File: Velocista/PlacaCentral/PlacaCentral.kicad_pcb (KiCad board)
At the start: 2 copper layers, 39 parts, among them J1 AUX1, J10 TB6612FNG_A, J11 MOT_IZQ, J12 MOT_DER, J13 DIST_DCHA, J14 TB6612FNG_B, J15 LIPO_1S_A, J16 LIPO_1S_B, J2 AUX2, J3 AUX3, J4 AUX4, J5 HC-05, J6 Sensores_linea, J7 DIST_IZQ, J8 DIST_FRONT, J9 LIPO_2S, SW1 B1, SW2 B2, SW3 SW_DPDT_x2, U1 PCF8574, U2 DC-DC_BuckModule

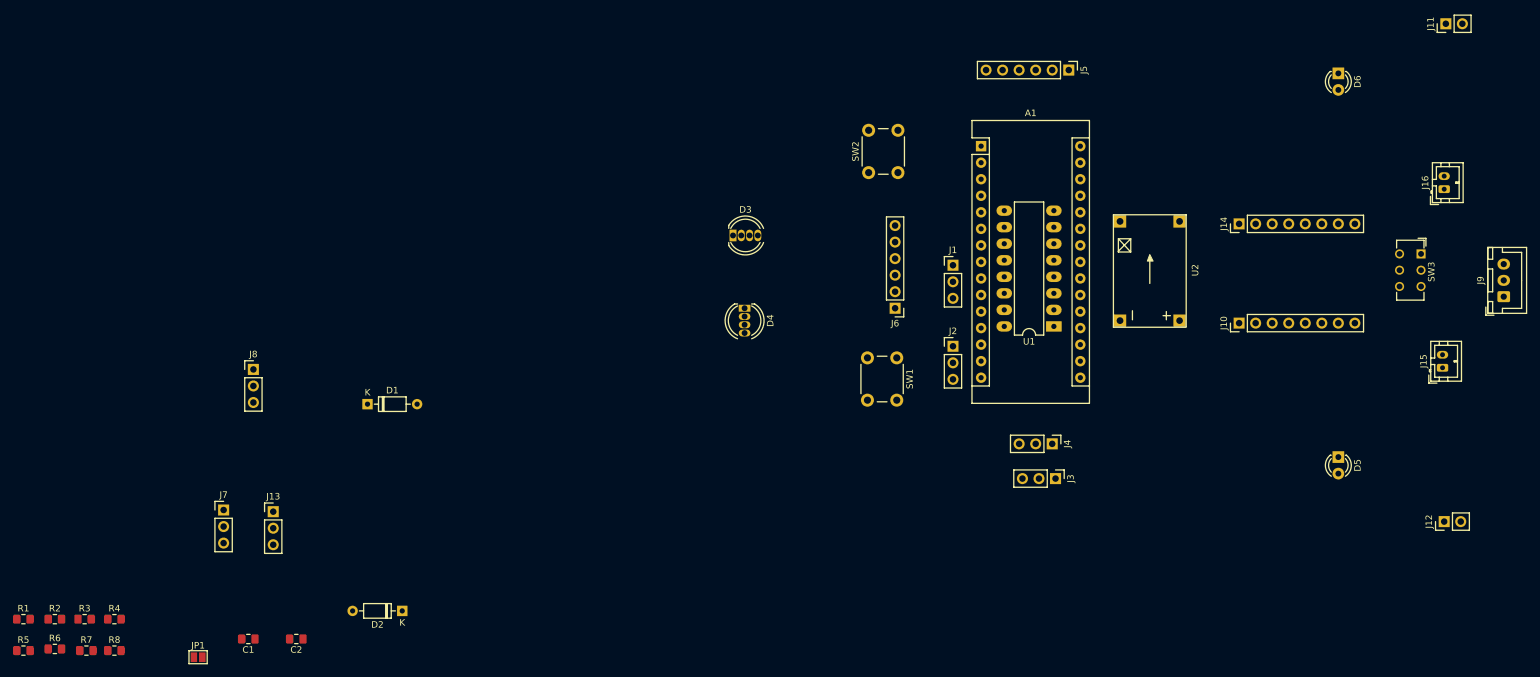
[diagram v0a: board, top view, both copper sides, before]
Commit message: Terminada distribución de componentes y enrutado
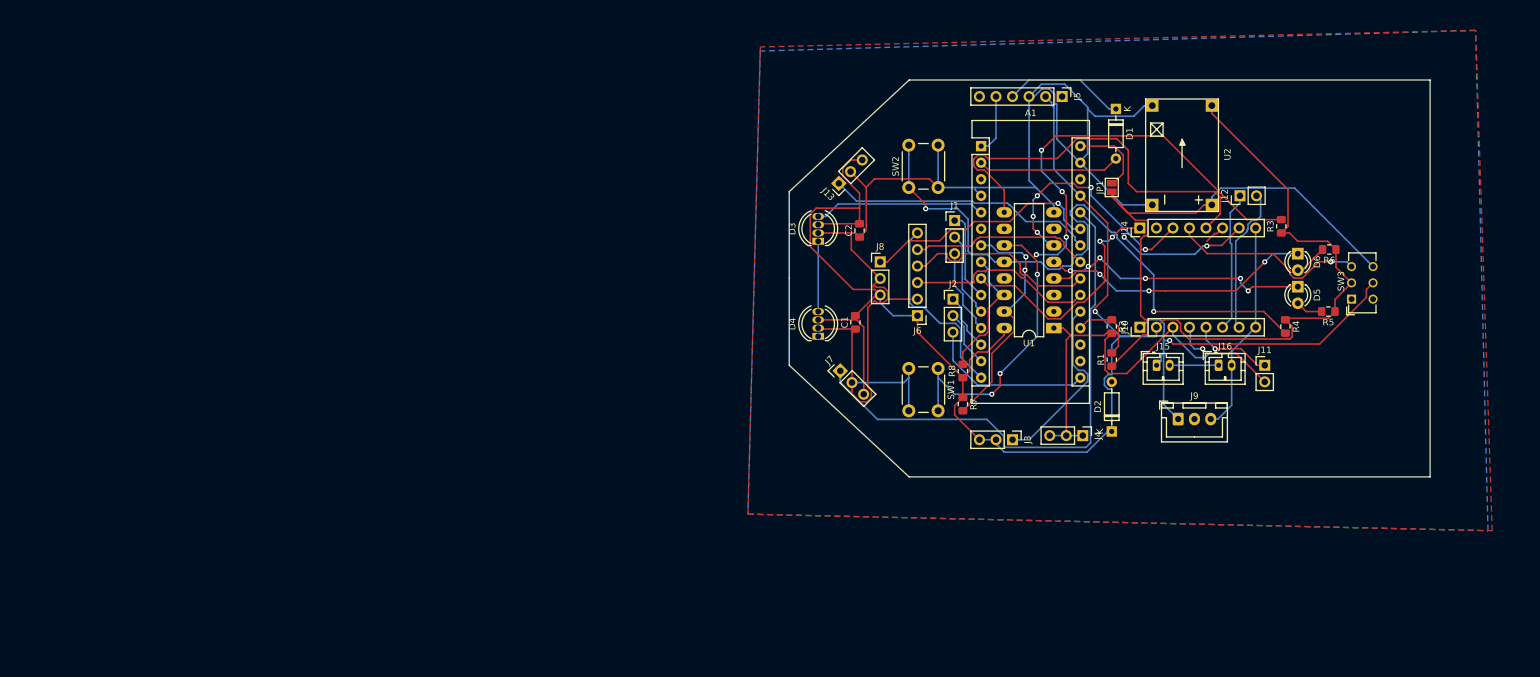
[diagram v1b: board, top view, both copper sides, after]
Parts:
- moved R5 207.1 mm to (217.4, 95.2), turned to 180 degrees
- moved R6 205.1 mm to (217.6, 85.7), turned to 180 degrees
- moved R3 193.4 mm to (210.2, 82.2), turned to 90 degrees
- moved R4 185.4 mm to (210.8, 97.5), turned to 270 degrees
- moved R1 171.8 mm to (184.2, 102.6), turned to 90 degrees
- moved R2 168.4 mm to (184.2, 97.5), turned to 270 degrees
- moved JP1 157.8 mm to (184.2, 76.2), turned to 90 degrees
- moved R7 139.8 mm to (161.3, 109.5), turned to 270 degrees
- moved R8 137.2 mm to (161.3, 104.4), turned to 90 degrees
- moved D1 123.6 mm to (184.8, 64.1), turned to 270 degrees
- moved D2 112.4 mm to (184.2, 113.7), turned to 90 degrees
- moved C2 106.9 mm to (145.4, 82.8), turned to 90 degrees
- moved C1 105.1 mm to (144.8, 96.9), turned to 90 degrees
- moved J13 100.4 mm to (142.2, 75.6), turned to 135 degrees
- moved J8 97.7 mm to (148.6, 87.6)
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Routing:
- net GND: track 0.00 -> 302.4 mm
- net +5V: track 0.00 -> 288.6 mm, vias 0 -> 1
- net B1: track 0.00 -> 110.3 mm, vias 0 -> 7
- net B2: track 0.00 -> 96.9 mm, vias 0 -> 2
- net DIST_IZQ: track 0.00 -> 82.1 mm
- net VDD: track 0.00 -> 81.1 mm
- net DIR_DER_1: track 0.00 -> 62.6 mm
- net VBAT: track 0.00 -> 59.4 mm, vias 0 -> 1
- net LED_R: track 0.00 -> 41.6 mm, vias 0 -> 6
- net LED_G: track 0.00 -> 41.6 mm, vias 0 -> 3
- net DIST_DCHA: track 0.00 -> 41.4 mm
- net DIR_IZQ_1: track 0.00 -> 37.9 mm, vias 0 -> 5
- net PWM_IZQ: track 0.00 -> 37.4 mm, vias 0 -> 2
- net DIST_FRONT: track 0.00 -> 37.0 mm, vias 0 -> 1
- net 12C_SDA: track 0.00 -> 37.0 mm, vias 0 -> 2
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- added copper zone on B.Cu, net GND
- added copper zone on F.Cu, net GND
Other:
- board outline added: 98.4 x 61 mm

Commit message: Terminado de enrutar
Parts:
- added REF**: MountingHole_2.2mm_M2, MountingHole:MountingHole_2.2mm_M2, F.Cu at (131.8, 100.8)
- added REF**: MountingHole_2.2mm_M2, MountingHole:MountingHole_2.2mm_M2, F.Cu at (131.8, 79.5)
- moved J5 1.70 mm to (178.1, 63.0)
- moved R8 0.51 mm to (160.8, 104.4)
- turned R7 to 90 degrees
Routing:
- net DIR_DER_2: track 3.25 -> 142.7 mm
- net DIST_DCHA: track 41.4 -> 124.8 mm
- net LINEA_3: track 27.8 -> 98.9 mm, vias 0 -> 7
- net +5V: track 288.6 -> 345.5 mm, vias 1 -> 4
- net PWM_DER: track 20.5 -> 73.9 mm, vias 2 -> 0
- net DIST_FRONT: track 37.0 -> 80.4 mm, vias 1 -> 3
- net LED_G: track 41.6 -> 82.1 mm
- net B1: track 110.3 -> 142.5 mm, vias 7 -> 1
- net DIST_IZQ: track 82.1 -> 112.2 mm, vias 0 -> 4
- net 12C_SCL: track 20.8 -> 40.1 mm
- net NEO: track 26.3 -> 44.4 mm
- net DIR_IZQ_2: track 0.00 -> 17.4 mm, vias 0 -> 3
- net M_DER_-: track 21.5 -> 38.5 mm
- net DIR_IZQ_1: track 37.9 -> 26.5 mm, vias 5 -> 3
- net GND: track 302.4 -> 291.3 mm, vias 0 -> 4
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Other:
- board size 98.4 x 61 mm -> 103.8 x 61 mm
